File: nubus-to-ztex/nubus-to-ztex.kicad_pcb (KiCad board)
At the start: 4 copper layers, 161.6 x 95.6 mm, 85 parts, among them J1 Conn_02x07_Odd_Even, J10 Conn_01x03_Male, J2 Conn_01x06_Male, J3 C96ABC, J4 DB15_Female_HighDensity_Mount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, J5 HDMI_A, J6 USB micro-B, J7 Conn_01x03_Male, J8 Conn_02x07_Odd_Even, J9 Conn_01x02, U1 74LVC1G07, U10 74FCT245ATQG, U11 74FCT245ATQG, U12 74FCT245ATQG, U2 AD1580, U4 ADV7125-lqfp48, U5 TPD12S016PWR, U6 SN65220, U7 TPS2051C, U8 XC9536XL-VQ44, U9 74FCT245ATQG

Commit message: large update
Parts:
- removed C33: 10uF, Capacitor_SMD:C_0805_2012Metric
- removed J10: Conn_01x03_Male, Connector_Molex:Molex_KK-254_AE-6410-03A_1x03_P2.54mm_Vertical
- removed U1: 74LVC1G07, Package_TO_SOT_SMD:SOT-23-5
- added D1: GREEN, LED_SMD:LED_0805_2012Metric, F.Cu at (123.3, 47.0)
- added D10: YELLOW, LED_SMD:LED_0805_2012Metric, F.Cu at (121.6, 56.7)
- added D11: YELLOW, LED_SMD:LED_0805_2012Metric, F.Cu at (121.6, 53.9)
- added D12: YELLOW, LED_SMD:LED_0805_2012Metric, F.Cu at (122.5, 60.1)
- added D13: YELLOW, LED_SMD:LED_0805_2012Metric, F.Cu at (126.1, 77.8)
- added D14: YELLOW, LED_SMD:LED_0805_2012Metric, F.Cu at (217.8, 60.8)
- added D15: YELLOW, LED_SMD:LED_0805_2012Metric, F.Cu at (217.8, 57.5)
- added D16: ORANGE, LED_SMD:LED_0805_2012Metric, F.Cu at (155.5, 18.8)
- added D17: ORANGE, LED_SMD:LED_0805_2012Metric, F.Cu at (155.5, 22.0)
- added D6: GREEN, LED_SMD:LED_0805_2012Metric, F.Cu at (123.3, 44.0)
- added D7: GREEN, LED_SMD:LED_0805_2012Metric, F.Cu at (123.3, 41.0)
- added D8: GREEN, LED_SMD:LED_0805_2012Metric, F.Cu at (123.3, 38.1)
- added D9: ORANGE, LED_SMD:LED_0805_2012Metric, F.Cu at (197.8, 78.2)
- added Q1: MMBT3904, Package_TO_SOT_SMD:SOT-23, F.Cu at (114.5, 97.0)
- added Q2: MMBT3904, Package_TO_SOT_SMD:SOT-23, F.Cu at (118.2, 89.8)
- added R21: 549, Resistor_SMD:R_0603_1608Metric, F.Cu at (119.5, 47.0)
- added R22: 549, Resistor_SMD:R_0603_1608Metric, F.Cu at (119.5, 44.0)
- added R27: 549, Resistor_SMD:R_0603_1608Metric, F.Cu at (119.5, 41.0)
- added R28: 549, Resistor_SMD:R_0603_1608Metric, F.Cu at (119.5, 38.1)
- added R29: 549, Resistor_SMD:R_0603_1608Metric, F.Cu at (197.8, 82.0)
- added R30: 549, Resistor_SMD:R_0603_1608Metric, F.Cu at (117.8, 56.7)
- added R31: 549, Resistor_SMD:R_0603_1608Metric, F.Cu at (117.8, 53.9)
- added R32: 549, Resistor_SMD:R_0603_1608Metric, F.Cu at (118.7, 60.2)
- added R33: 549, Resistor_SMD:R_0603_1608Metric, F.Cu at (125.1, 74.9)
- added R34: 549, Resistor_SMD:R_0603_1608Metric, F.Cu at (221.8, 60.8)
- added R35: 549, Resistor_SMD:R_0603_1608Metric, F.Cu at (221.8, 57.5)
- added R36: 549, Resistor_SMD:R_0603_1608Metric, F.Cu at (159.5, 18.8)
- added R37: 549, Resistor_SMD:R_0603_1608Metric, F.Cu at (159.5, 22.0)
- added R38: 1k, Resistor_SMD:R_0603_1608Metric, F.Cu at (113.5, 93.5)
- added R39: 27, Resistor_SMD:R_0603_1608Metric, F.Cu at (119.0, 86.2)
- added R40: 1k, Resistor_SMD:R_0603_1608Metric, F.Cu at (117.2, 86.2)
- C26: value 100nF -> 1uF
- R17: value 10k -> 27
- U10, U11, U12, U9: footprint Package_SO:QSOP-20_3.9x8.7mm_P0.635mm -> For_SeeedStudio:QSOP-20_3.9x8.7mm_P0.635mm_Renesas
- moved R17 28.3 mm to (115.2, 93.5), turned to 90 degrees
- moved C12 24.7 mm to (259.5, 53.8)
- moved C13 24.7 mm to (256.3, 54.6)
- moved C21 24.7 mm to (253.8, 53.0)
- moved U5 24.7 mm to (250.9, 59.0)
- moved C14 24.5 mm to (244.9, 61.1), turned to 90 degrees
- moved C26 2.10 mm to (125.8, 71.0), turned to 90 degrees
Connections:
- net ~NMRQ_3V3 renamed NMRQ
- JAB1 pad 16: fpga_to_cpld_signal_2 -> Net-(JAB1-Pad16)
- R17 pad 1: +3V3 -> Net-(Q1-Pad1)
- U8 pad 40: fpga_to_cpld_signal_2 -> ~RQST_5V
- U8 pad 43: ~RQST_5V -> RQST_o
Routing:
- net +3V3: track 474.6 -> 577.0 mm, vias 18 -> 23
- net FPGA_G4: track 39.0 -> 90.0 mm
- net FPGA_G3: track 40.6 -> 90.0 mm
- net FPGA_G5: track 41.7 -> 90.0 mm
- net FPGA_G2: track 43.2 -> 90.0 mm
- net ARB: track 14.0 -> 60.1 mm, vias 0 -> 1
- net FPGA_G6: track 44.5 -> 90.0 mm
- net GRANT: track 11.1 -> 56.5 mm, vias 0 -> 1
- net FPGA_G1: track 45.8 -> 90.0 mm
- net FPGA_G7: track 47.2 -> 90.0 mm
- net FPGA_G0: track 48.4 -> 90.0 mm
- net FPGA_R7: track 52.4 -> 90.0 mm
- net FPGA_R6: track 55.7 -> 90.0 mm
- net FPGA_B0: track 56.1 -> 90.0 mm
- net GND: track 1147.6 -> 1180.1 mm, vias 43 -> 46
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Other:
- board size 161.6 x 95.6 mm -> 161.6 x 100.1 mm
- board text added: "ACK"
- board text added: "AD0/1"
- board text added: "ARB GRANT"
- board text added: "Nubus OE"
- board text added: "Slot ID"
- board text added: "Start"
- board text added: "TM0/1"
- board text added: "USER LED 0..3"
- board text removed: "+12V"
- board text removed: "Fan 12V 1.5W"
- board text removed: "LED 0..3"

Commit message: another update after discussion on tinkerdifferent
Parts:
- removed D4, D5: RED, LED_SMD:LED_0805_2012Metric
- removed Q1, Q2: MMBT3904, Package_TO_SOT_SMD:SOT-23
- removed R10, R9: 549, Resistor_SMD:R_0603_1608Metric
- removed R17, R39: 27, Resistor_SMD:R_0603_1608Metric
- removed R38, R40: 1k, Resistor_SMD:R_0603_1608Metric
- added C33: 10nF, Capacitor_SMD:C_0603_1608Metric, F.Cu at (135.9, 86.8)
- added C34: 100nF, Capacitor_SMD:C_0603_1608Metric, F.Cu at (135.9, 85.1)
- added C35: 100nF, Capacitor_SMD:C_0603_1608Metric, F.Cu at (138.7, 90.1)
- added C36: 100nF, Capacitor_SMD:C_0603_1608Metric, F.Cu at (118.5, 85.5)
- added U1: XC9572XL-VQ64, For_SeeedStudio:TQFP-64_10x10mm_P0.5mm_Xlinx, F.Cu at (136.2, 76.2)
- added U3: 74LVC125, Package_SO:TSSOP-14_4.4x5mm_P0.65mm, F.Cu at (143.8, 88.8)
- U8: value XC9536XL-VQ44 -> 74LVC125; footprint For_SeeedStudio:TQFP-44_10x10mm_P0.8mm_Xilinx -> Package_SO:TSSOP-14_4.4x5mm_P0.65mm
- moved U8 24.2 mm to (116.0, 89.5), turned to 0 degrees
- moved D12 7.86 mm to (123.5, 52.3)
- moved R32 7.86 mm to (119.7, 52.4)
- moved R23 5.75 mm to (133.5, 86.0)
- moved R24 5.75 mm to (131.7, 86.0)
- moved R25 5.75 mm to (129.9, 86.0)
- moved R26 5.75 mm to (128.1, 86.0)
- moved D10 4.05 mm to (123.8, 60.1)
- moved D11 4.05 mm to (123.8, 57.3)
- moved R30 4.05 mm to (120.0, 60.1)
- moved R31 4.05 mm to (120.0, 57.3)
- moved D13 2.69 mm to (127.5, 75.5)
- moved C30 1.88 mm to (139.9, 66.7)
- moved C22 1.80 mm to (138.1, 68.4)
- moved C1 1.73 mm to (127.8, 73.5), turned to 180 degrees
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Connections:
- JAB1 pad 16: Net-(JAB1-Pad16) -> fpga_to_cpld_signal_2
- JAB1 pad 6: NMRQ -> ~NMRQ_3V3
- JCD1 pad 16: LED2 -> ~CLK2X_3V3
- JCD1 pad 18: LED3 -> ~TM2_3V3
- U8 pad 1: fpga_to_cpld_clk -> +3V3
- U8 pad 10: CPLD_JTAG_TMS -> ~NMRQ_3V3
- U8 pad 11: CPLD_JTAG_TCK -> ~RQST_5V
- U8 pad 12: ~ARB0_5V -> GND
- U8 pad 13: ~ARB1_5V -> RQST_o_n
- U8 pad 14: ~ARB2_5V -> +3V3
- U8 pad 2: ~START_5V -> GND
- U8 pad 3: ~ACK_5V -> Net-(U8-Pad3)
- U8 pad 4: GND -> +3V3
- U8 pad 5: ~ID3_5V -> GND
- U8 pad 6: ~ID2_5V -> Net-(U8-Pad6)
- U8 pad 7: ~ID1_5V -> GND
- U8 pad 8: ~ID0_5V -> ~NMRQ_5V
- U8 pad 9: CPLD_JTAG_TDI -> GND
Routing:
- net +3V3: track 577.0 -> 648.1 mm, vias 23 -> 30
- net ~TM2_5V: track 0.00 -> 57.0 mm, vias 0 -> 1
- net ~TM2_3V3: track 0.00 -> 53.6 mm
- net ~CLK2X_3V3: track 0.00 -> 51.9 mm
- net NMRQ: track 42.7 -> 0.00 mm
- net ~NMRQ_3V3: track 0.00 -> 42.0 mm
- net ~CLK2X_5V: track 0.00 -> 23.3 mm, vias 0 -> 1
- net RQST_o_n: track 0.00 -> 17.6 mm
- net fpga_to_cpld_signal_2: track 0.00 -> 15.1 mm
- net ARB0_o_n: track 0.00 -> 14.1 mm
- net RQST_o: track 14.0 -> 0.00 mm
- net ARB1_o_n: track 0.00 -> 13.2 mm
- net ARB2_o_n: track 0.00 -> 12.5 mm
- net ~TM0_5V: track 67.8 -> 56.4 mm
- net ~TM1_5V: track 72.1 -> 61.0 mm
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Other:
- board text added: "USER LED 0..1"
- board text removed: "Start"
- board text removed: "USER LED 0..3"

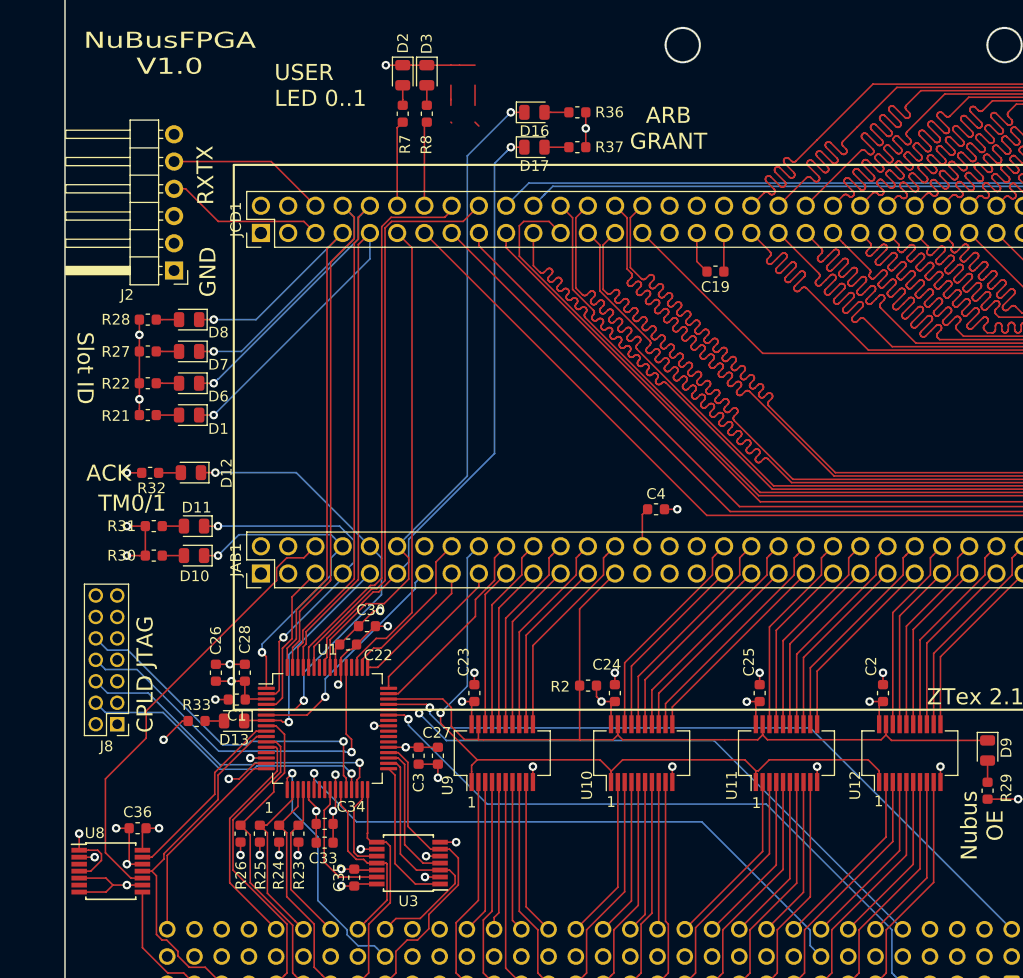
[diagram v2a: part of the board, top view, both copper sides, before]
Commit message: Switch from 5V 74FCT245 to 3.3V 74LVT245
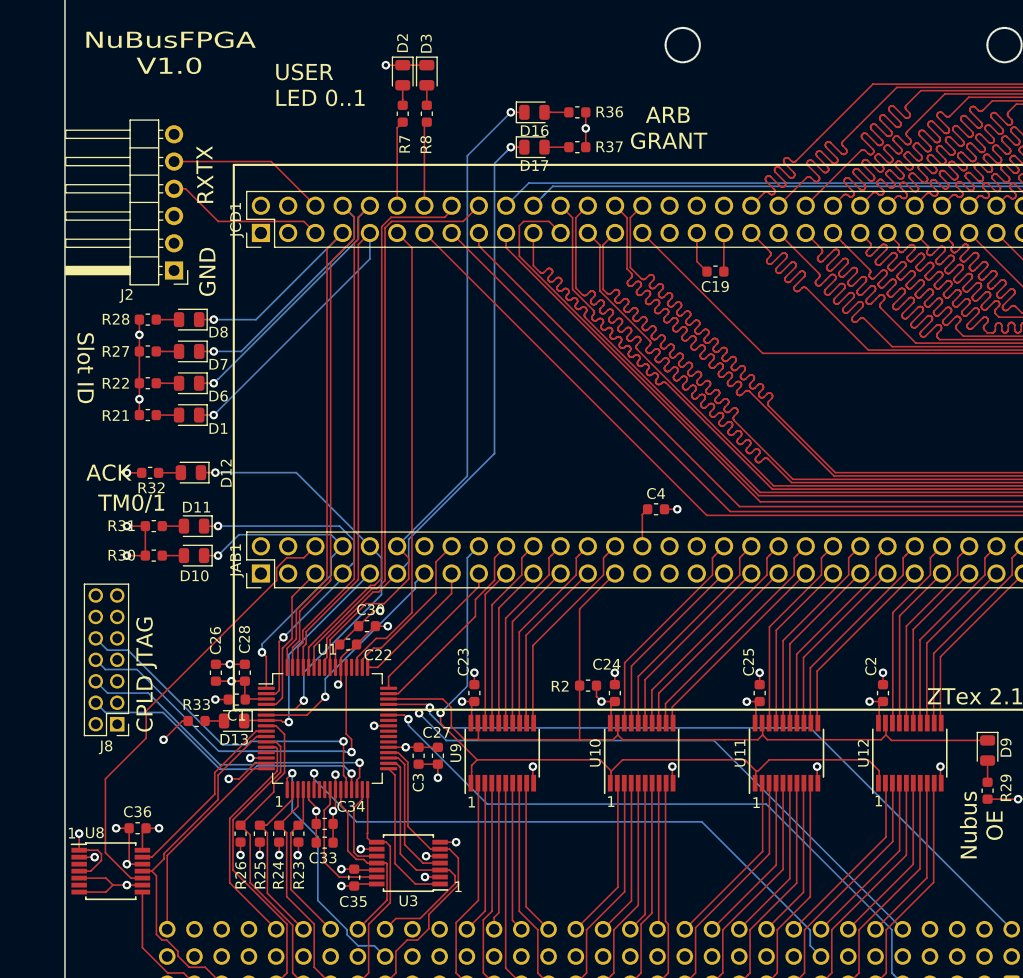
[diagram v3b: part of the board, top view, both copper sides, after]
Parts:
- U10, U11, U12, U9: value 74FCT245ATQG -> 74LVT245PW,118; footprint For_SeeedStudio:QSOP-20_3.9x8.7mm_P0.635mm_Renesas -> For_SeeedStudio:TSSOP-20_4.4x6.5mm_P0.65mm_ForSeeedStudio
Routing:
- net Net-(D5-Pad2): track 1.87 -> 0.00 mm
- net Net-(D4-Pad2): track 1.87 -> 0.00 mm
- net LED3: track 0.51 -> 0.00 mm

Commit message: large clean-up update
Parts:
- removed the D9 at (197.8, 78.2)
- removed the R29 at (197.8, 82.0)
- added C3: 47uF 10V+, Capacitor_SMD:C_0805_2012Metric, F.Cu at (131.3, 56.1)
- added C38: 1uF, Capacitor_SMD:C_0603_1608Metric, F.Cu at (235.6, 36.6)
- added C5: 100nF, Capacitor_SMD:C_0603_1608Metric, F.Cu at (182.5, 72.9)
- added D10: YELLOW, LED_SMD:LED_0805_2012Metric, F.Cu at (155.5, 14.7)
- added D3: BLUE, LED_SMD:LED_0805_2012Metric, F.Cu at (114.8, 15.5)
- added R15: 549, Resistor_SMD:R_0603_1608Metric, F.Cu at (159.0, 14.7)
- added R3: 549, Resistor_SMD:R_0603_1608Metric, F.Cu at (114.8, 12.0)
- added U2: 74LVT125, Package_SO:TSSOP-14_4.4x5mm_P0.65mm, F.Cu at (184.5, 78.5)
- U1: renamed from U8; value 74LVC125 -> 74LVT125
- U3: value 74LVC125 -> 74LVT125
- U5: renamed from U9; value 74LVT245PW,118 -> 74LVT245BPW,118
- U6: renamed from U10; value 74LVT245PW,118 -> 74LVT245BPW,118
- U7: renamed from U11; value 74LVT245PW,118 -> 74LVT245BPW,118
- U8: renamed from U12; value 74LVT245PW,118 -> 74LVT245BPW,118
- moved R14 3.35 mm to (124.0, 72.2), turned to 270 degrees
- moved D9 3.20 mm to (124.3, 75.0)
- moved C18 2.00 mm to (174.5, 72.9)
- moved U7 2.00 mm to (177.0, 78.5)
- moved C35 1.63 mm to (238.8, 37.7)
- moved C19 1.50 mm to (189.5, 72.9)
- moved U8 1.50 mm to (192.0, 78.5)
- moved C4 1.00 mm to (119.2, 84.8)
- moved U1 1.00 mm to (116.7, 88.8)
- moved C29 0.54 mm to (204.1, 82.2)
- moved C12 0.50 mm to (139.7, 66.2)
- moved C32 0.48 mm to (238.8, 35.5)
- moved C8 0.47 mm to (138.1, 67.9)
- moved R35 0.44 mm to (253.9, 36.9)
- moved R34 0.37 mm to (253.9, 35.1)
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- renumbered C19 to C1, C27 to C10, C28 to C11, C30 to C12, C26 to C13, C23 to C14, C33 to C15, C34 to C16, C24 to C17, C25 to C18, C2 to C19, C4 to C2, C21 to C20, C12 to C21, C13 to C22, C14 to C23, C15 to C24, C16 to C25, C17 to C26, C18 to C27, C20 to C28, C31 to C29, C32 to C30, C7 to C31, C6 to C32, C29 to C33, C8 to C34, C9 to C35, C5 to C36, C10 to C37, C11 to C39, C36 to C4, C35 to C6, C3 to C7, C22 to C8, C1 to C9, D2 to D1, D1 to D11, D6 to D12, D7 to D13, D8 to D14, D14 to D15, D15 to D16, D3 to D2, D16 to D4, D17 to D5, D10 to D6, D11 to D7, D12 to D8, D13 to D9, J8 to J2, J2 to J3, J3 to J4, J9 to J8, J4 to J9, R7 to R1, R37 to R10, R30 to R11, R31 to R12, R32 to R13, R33 to R14, R21 to R16, R22 to R17, R27 to R18, R28 to R19, R8 to R2, R34 to R20, R35 to R21, R11 to R22, R12 to R23, R13 to R24, R14 to R25, R15 to R26, R16 to R27, R3 to R28, R20 to R29, R1 to R30, R18 to R31, R19 to R32, R4 to R33, R5 to R34, R6 to R35, R2 to R4, R23 to R5, R24 to R6, R25 to R7, R26 to R8, R36 to R9, U6 to U10, U7 to U11, U4 to U12, U2 to U13, U1 to U4, U5 to U9
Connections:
- R8 pad 1: +5V -> ~ID3_5V
- R8 pad 2: ~ID3_5V -> +5V
- U1 pad 1: +3V3 -> ~NMRQ_3V3
- U1 pad 10: ~NMRQ_3V3 -> START_oe_n
- U1 pad 11: ~RQST_5V -> ~ACK_5V
- U1 pad 12: GND -> ACK_o_n
- U1 pad 13: RQST_o_n -> ACK_oe_n
- U1 pad 3: Net-(U8-Pad3) -> ~NMRQ_5V
- U1 pad 4: +3V3 -> RQST_o_n
- U1 pad 6: Net-(U8-Pad6) -> ~RQST_5V
- U1 pad 8: ~NMRQ_5V -> ~START_5V
- U1 pad 9: GND -> START_o_n
- U4 pad 1: ~TM1_3V3 -> ~ID3_3V3
- U4 pad 10: ~RQST_5V -> ~ACK_5V
- U4 pad 11: ~ACK_5V -> START_oe_n
- U4 pad 12: ~START_5V -> START_o_n
- U4 pad 13: Net-(U1-Pad13) -> ~START_5V
- U4 pad 2: ~TM0_3V3 -> ~ACK_3V3
- U4 pad 23: Net-(U1-Pad23) -> fpga_to_cpld_signal
- U4 pad 24: Net-(U1-Pad24) -> TM2_oe_n
- U4 pad 38: Net-(U1-Pad38) -> ~TM1_5V
- U4 pad 39: Net-(U1-Pad39) -> ~TM0_5V
- U4 pad 4: ~RQST_3V3 -> ~START_3V3
- U4 pad 40: Net-(U1-Pad40) -> TM1_n_o
- U4 pad 42: Net-(U1-Pad42) -> TM0_n_o
- U4 pad 43: ~TM1_5V -> TMx_oe_n
- U4 pad 44: ~TM0_5V -> ~RESET_5V
- U4 pad 45: ~RESET_5V -> NUBUS_OE
- U4 pad 46: NUBUS_OE -> TM2_o_n
- U4 pad 5: ~ACK_3V3 -> RQST_o_n
- U4 pad 52: Net-(U1-Pad52) -> ARB
- U4 pad 56: ARB -> GRANT
- U4 pad 57: GRANT -> ~TM2_3V3
- U4 pad 58: Net-(U1-Pad58) -> ~CLK2X_3V3
- U4 pad 59: ~TM2_3V3 -> ~ID0_3V3
- U4 pad 6: fpga_to_cpld_signal -> ~RQST_5V
- U4 pad 60: ~CLK2X_3V3 -> ~ID1_3V3
- U4 pad 61: ~ID0_3V3 -> ~TM0_3V3
- U4 pad 62: ~ID1_3V3 -> ~TM1_3V3
- U4 pad 64: ~ID3_3V3 -> ~RQST_3V3
- U4 pad 7: ~START_3V3 -> ~ID3_5V
- U4 pad 8: ~ID3_5V -> ACK_oe_n
- U4 pad 9: RQST_o_n -> ACK_o_n
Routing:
- net TM2_oe_n: track 0.00 -> 59.1 mm, vias 0 -> 3
- net ~RESET_3V3: track 14.2 -> 66.5 mm, vias 0 -> 1
- net TM2_o_n: track 0.00 -> 49.7 mm, vias 0 -> 2
- net GND: track 1187.1 -> 1236.2 mm, vias 52 -> 55
- net TM0_n_o: track 0.00 -> 47.8 mm, vias 0 -> 2
- net TMx_oe_n: track 0.00 -> 47.6 mm, vias 0 -> 2
- net TM1_n_o: track 0.00 -> 45.4 mm, vias 0 -> 2
- net +3V3: track 648.1 -> 680.5 mm, vias 30 -> 28
- net ~TM2_5V: track 57.0 -> 77.5 mm, vias 1 -> 3
- net START_o_n: track 0.00 -> 19.5 mm
- net START_oe_n: track 0.00 -> 19.3 mm
- net ACK_o_n: track 0.00 -> 18.6 mm
- net ACK_oe_n: track 0.00 -> 18.3 mm
- net ~START_5V: track 21.6 -> 36.9 mm
- net ~ACK_5V: track 28.0 -> 41.6 mm
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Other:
- board size 161.6 x 100.1 mm -> 161.6 x 100 mm
- board text added: "3.3V Power ON"
- board text added: "A"
- board text added: "B"
- board text added: "C"
- board text added: "Reset"
- board text added: "START"
- board text added: "User LED 0..1"
- board text removed: "Nubus OE"
- board text removed: "USER LED 0..1"

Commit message: more updates
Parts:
- added R36: 10k, Resistor_SMD:R_0603_1608Metric, F.Cu at (114.4, 83.7)
- added R37: 10k, Resistor_SMD:R_0603_1608Metric, F.Cu at (120.3, 79.8)
- added R38: 10k, Resistor_SMD:R_0603_1608Metric, F.Cu at (125.5, 83.3)
- added R39: 10k, Resistor_SMD:R_0603_1608Metric, F.Cu at (121.4, 82.7)
- added R40: 10k, Resistor_SMD:R_0603_1608Metric, F.Cu at (182.1, 85.1)
- added R41: 10k, Resistor_SMD:R_0603_1608Metric, F.Cu at (186.1, 71.3)
- added R42: 10k, Resistor_SMD:R_0603_1608Metric, F.Cu at (143.0, 84.9)
- added R43: 10k, Resistor_SMD:R_0603_1608Metric, F.Cu at (144.6, 83.2)
- added R44: 10k, Resistor_SMD:R_0603_1608Metric, F.Cu at (135.9, 89.6)
- added R45: 10k, Resistor_SMD:R_0603_1608Metric, F.Cu at (139.6, 84.9)
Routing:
- net +3V3: track 680.5 -> 742.7 mm, vias 28 -> 34
- net GND: track 1236.2 -> 1251.8 mm
- net TMx_oe_n: track 47.6 -> 50.7 mm
- net TM2_oe_n: track 59.1 -> 61.8 mm
- net RQST_o_n: track 25.1 -> 26.4 mm
- net ACK_oe_n: track 18.3 -> 19.3 mm
- net ~ARB1_5V: track 29.4 -> 30.2 mm
- net ARB1_o_n: track 13.2 -> 13.8 mm

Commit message: some missing stuff, minor HW update, SW
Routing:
- net GND: track 1251.8 -> 1359.9 mm, vias 55 -> 65
- added copper zone on B.Cu, net GND
- added copper zone on F.Cu, net GND
